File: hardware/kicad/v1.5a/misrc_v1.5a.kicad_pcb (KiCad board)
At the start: 2 copper layers, 146.2 x 72.6 mm, 194 parts, among them J1 Conn_01x01_Shielded, J2 Conn_01x08_Socket, J201 DOSIN-801-0050, J3 GPIFII_J6, J4 GPIFII_J7, Q1 FZT690B, Q101 CMPT5179, Q102 CMPT5179, Q2 FZT790A, Q201 CMPT5179, Q202 CMPT5179, SW1 SW_Push, SW101 SW_DIP_x04, SW102 SW_DIP_x03, SW103 SW_DIP_x03, SW104 SW_DIP_x03, SW105 SW_DIP_x02, SW2 SW_DIP_x01, SW201 SW_DIP_x04, SW202 SW_DIP_x03, SW203 SW_DIP_x03, SW204 SW_DIP_x03, SW205 SW_DIP_x02, U1 4043, U101 AD8138ARZ, U102 AD9235, U2 74VHC541, U201 AD8138ARZ, U202 AD9235, U3 74VHC541, U4 74VHC541, U5 74VHC541, U6 TPS60401, U7 ADP7156ARDZ, X1 40M

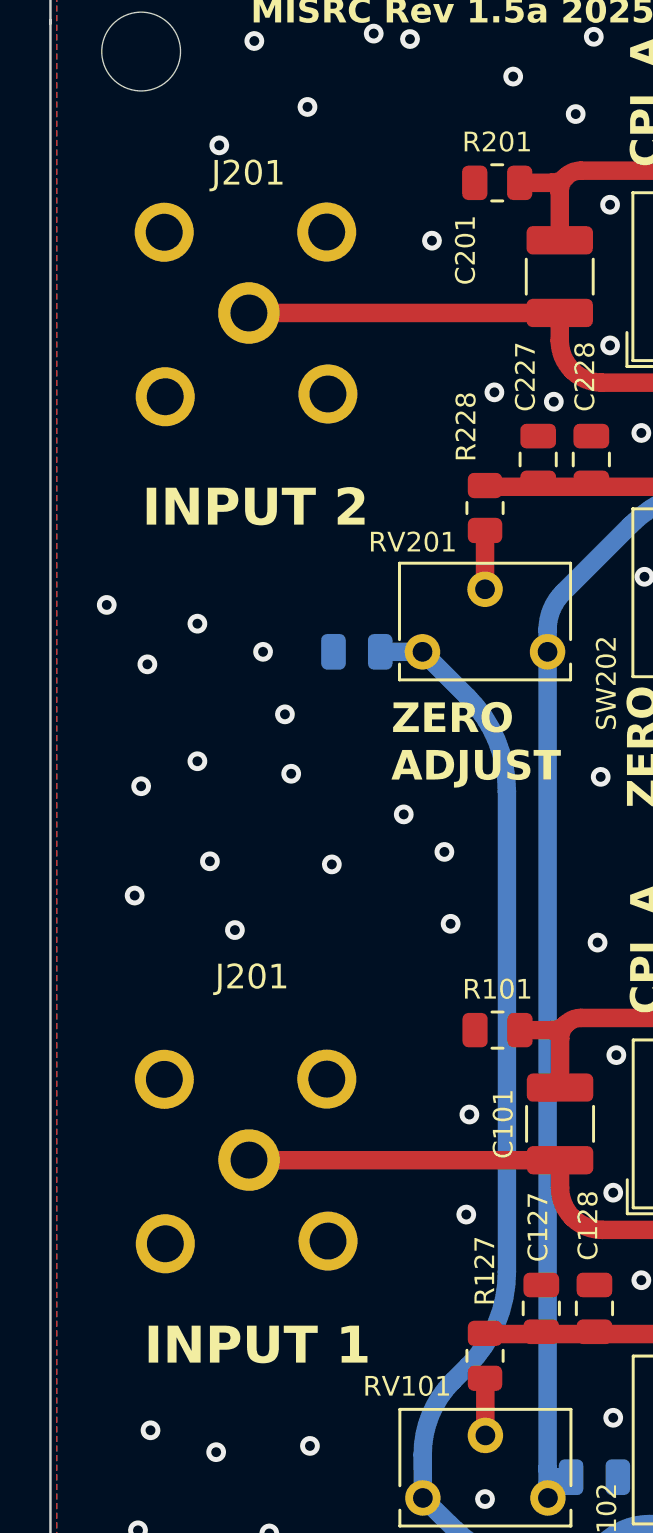
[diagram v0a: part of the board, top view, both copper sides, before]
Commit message: silkscreen positions
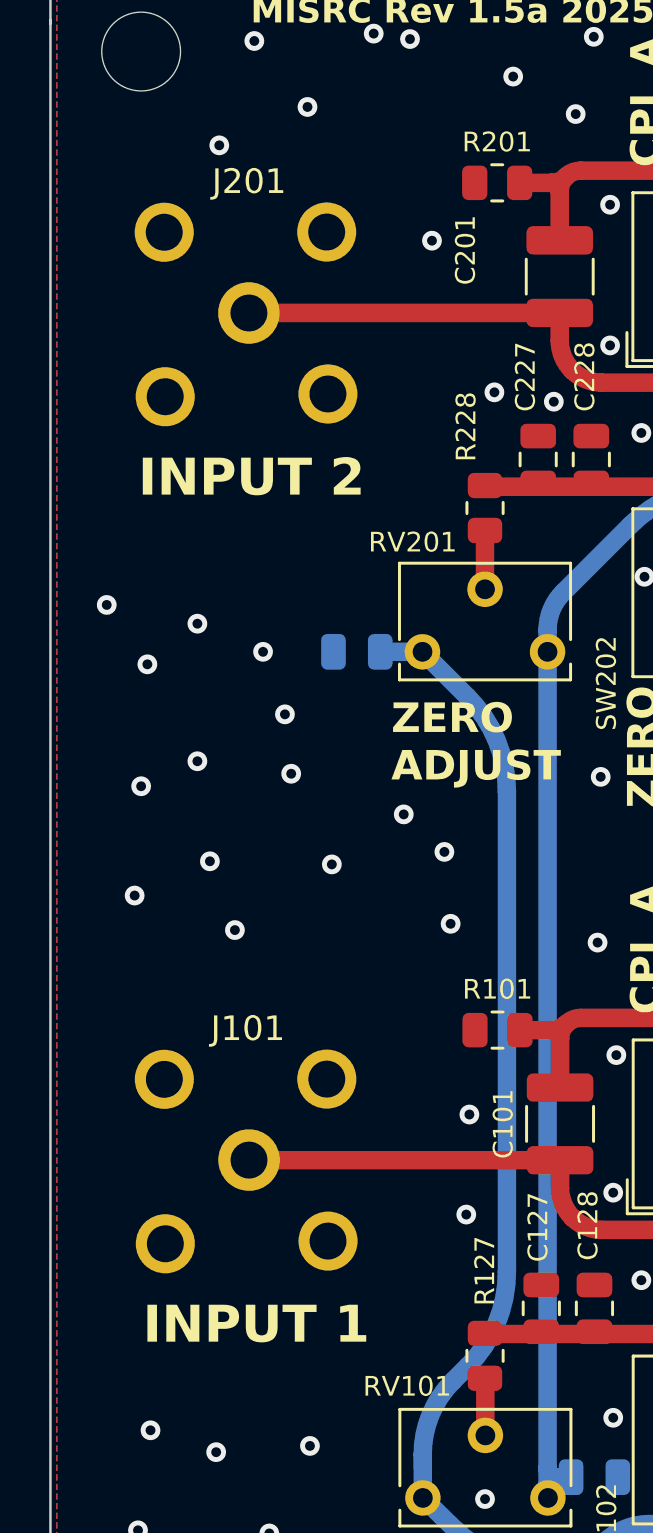
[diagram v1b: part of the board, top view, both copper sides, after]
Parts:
- renumbered J201 to J101
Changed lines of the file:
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@@
 		(tags "BNC female PCB mount 4 pin straight chassis connector ")
 		(property "Reference" "J201"
-			(at -0.02 -5.68 0)
+			(at 0.01 -5.34 0)
 			(layer "F.SilkS")
 			(effects
@@
 		)
 		(property "Value" "DOSIN-801-0050"
-			(at 0.31 -1.69 0)
+			(at 0.55 -2.01 0)
 			(layer "F.Fab")
 			(effects
@@
 		(descr "BNC female PCB mount 4 pin straight chassis connector http://www.te.com/usa-en/product-1-1478204-0.html")
 		(tags "BNC female PCB mount 4 pin straight chassis connector ")
-		(property "Reference" "J201"
-			(at 0.125 -7.44 0)
+		(property "Reference" "J101"
+			(at -0.045 -5.34 0)
 			(layer "F.SilkS")
 			(effects
@@
 		)
 		(property "Value" "DOSIN-801-0050"
-			(at 0.02 -5.67 0)
+			(at -0.265 -2.32 0)
 			(layer "F.Fab")
 			(effects
@@
 	)
 	(gr_text "INPUT 2"
-		(at 64.3 86.33 0)
+		(at 64.14 85.11 0)
 		(layer "F.SilkS")
 		(effects
@@
 	)
 	(gr_text "INPUT 1"
-		(at 64.38 120.37 0)
+		(at 64.33 119.52 0)
 		(layer "F.SilkS")
 		(effects

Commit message: Fix J201 pad path, causing production issues with fabs
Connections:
- J201 pad 1: Net-(J101-Signal) -> Net-(J201-Signal)
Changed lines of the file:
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@@
 			(layers "*.Cu" "*.Mask")
 			(remove_unused_layers no)
-			(net 50 "Net-(J101-Signal)")
+			(net 66 "Net-(J201-Signal)")
 		)
 		(pad "2" thru_hole circle
